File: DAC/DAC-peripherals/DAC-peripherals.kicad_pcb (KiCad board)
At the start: 2 copper layers, 46 parts, among them IC1 THS8135PHP, J1 Conn_01x04_Female, J2 Conn_01x02_Female, J3 Conn_01x11_Female, J4 Conn_01x11_Female, J5 Conn_01x11_Female, J6 Conn_01x01_Female, J7 Conn_01x01_Female, U1 SN74LV1T34DBV, U10 74LVC2T45DC, U11 74LVC2T45DC, U12 74LVC2T45DC, U13 74LVC2T45DC, U14 74LVC2T45DC, U15 74LVC2T45DC, U16 74LVC2T45DC, U2 74LVC2T45DC, U3 74LVC2T45DC, U4 74LVC2T45DC, U5 74LVC2T45DC, U6 74LVC2T45DC, U7 74LVC2T45DC, U8 74LVC2T45DC, U9 74LVC2T45DC

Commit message: improved PCB design
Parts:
- removed C10, C11, C12, C13, C14, C15, C16, C17, C18, C8, C9: C, Capacitor_SMD:C_0805_2012Metric
- removed J6, J7: Conn_01x01_Female, Connector_PinHeader_2.54mm:PinHeader_1x01_P2.54mm_Vertical
- removed U16: 74LVC2T45DC, Package_SO:VSSOP-8_2.3x2mm_P0.5mm
- added Q21: Q_NMOS_DGS, Package_TO_SOT_SMD:SOT-23, F.Cu at (122.2, 90.2)
- added R45: 10K, Resistor_SMD:R_0603_1608Metric, F.Cu at (120.2, 92.7)
- added R46: 10K, Resistor_SMD:R_0603_1608Metric, F.Cu at (121.9, 87.6)
- C1, C5, C6, C7: value C -> 100n; footprint Capacitor_SMD:C_0805_2012Metric -> Capacitor_SMD:C_0603_1608Metric
- C2, C3: value 0.1u -> 100n; footprint Capacitor_SMD:C_0805_2012Metric -> Capacitor_SMD:C_0603_1608Metric
- C4: value C -> 4.7u; footprint Capacitor_SMD:C_0805_2012Metric -> Capacitor_SMD:C_0603_1608Metric
- IC1: footprint THS8135PHP:QFP50P900X900X120-49N -> Package_QFP:TQFP-48-1EP_7x7mm_P0.5mm_EP5x5mm
- J1: value Conn_01x04_Female -> Conn_01x03_Female; footprint Connector_PinHeader_2.54mm:PinHeader_1x04_P2.54mm_Vertical -> Connector_PinSocket_2.54mm:PinSocket_1x03_P2.54mm_Vertical
- J2: value Conn_01x02_Female -> Conn_01x03_Female; footprint Connector_PinHeader_2.54mm:PinHeader_1x02_P2.54mm_Vertical -> Connector_PinSocket_2.54mm:PinSocket_1x03_P2.54mm_Vertical
- J3, J4: value Conn_01x11_Female -> Conn_01x10_Female; footprint Connector_PinHeader_2.54mm:PinHeader_1x11_P2.54mm_Vertical -> Connector_PinSocket_2.54mm:PinSocket_1x10_P2.54mm_Vertical
- J5: value Conn_01x11_Female -> Conn_01x08_Female; footprint Connector_PinHeader_2.54mm:PinHeader_1x11_P2.54mm_Vertical -> Connector_PinSocket_2.54mm:PinSocket_1x08_P2.54mm_Vertical
- R1: value 37.5 -> 2k; footprint Resistor_SMD:R_0805_2012Metric -> Resistor_SMD:R_0603_1608Metric
- R2, R3, R4: value NC -> 75; footprint Resistor_SMD:R_0805_2012Metric -> Resistor_SMD:R_0603_1608Metric
- U1: value SN74LV1T34DBV -> LK112M18TR
- moved J4 96.8 mm to (151.1, 112.5), turned to 180 degrees
- moved U2 89.7 mm to (143.8, 116.6), turned to -90 degrees
- moved U6 89.2 mm to (133.6, 116.6), turned to -90 degrees
- moved U5 88.8 mm to (146.1, 95.8), turned to 0 degrees
- moved U4 88.7 mm to (138.7, 116.6), turned to -90 degrees
- moved U3 87.9 mm to (146.1, 90.9), turned to 0 degrees
- moved U7 81.7 mm to (146.1, 100.8), turned to 0 degrees
- moved C6 79.4 mm to (138.4, 97.3)
- moved C5 76.5 mm to (137.7, 94.7), turned to 180 degrees
- moved U9 74.6 mm to (146.1, 106.2), turned to 0 degrees
- moved J3 74.3 mm to (122.2, 121.9), turned to 90 degrees
- moved U8 72.3 mm to (128.5, 116.6), turned to -90 degrees
- moved C1 71.5 mm to (132.3, 94.8), turned to 90 degrees
- moved U11 67.3 mm to (146.1, 111.0), turned to 0 degrees
- moved U10 61.2 mm to (123.4, 116.6), turned to -90 degrees
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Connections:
- net Net-(J3-Pad7) renamed /level_shifter_parallell_inv/level_shifter_2channel2/in2
- net Net-(J5-Pad5) renamed /level_shifter_parallell8/level_shifter_2channel7/in2
- C2 pad 2: Net-(C2-Pad2) -> GND
- C3 pad 1: GND -> +1V8
- C3 pad 2: Net-(C3-Pad2) -> GND
- C5 pad 2: GND -> Net-(C5-Pad2)
- C6 pad 1: +3.3V -> Net-(C6-Pad1)
- C7 pad 1: +3.3V -> Net-(C7-Pad1)
- IC1 pad 1: /Level Shifter B/B9 -> /B8
- IC1 pad 10: /Level Shifter B/B10 -> GND
- IC1 pad 11: GND -> +1V8
- IC1 pad 12: +1V8 -> GND
- IC1 pad 13: /Level Shifter R/B1 -> /R1
- IC1 pad 14: /Level Shifter R/B2 -> /R2
- IC1 pad 15: /Level Shifter R/B3 -> /R3
- IC1 pad 16: /Level Shifter R/B4 -> /R4
- IC1 pad 17: /Level Shifter R/B5 -> /R5
- IC1 pad 18: /Level Shifter R/B6 -> /R6
- IC1 pad 19: /Level Shifter R/B7 -> /R7
- IC1 pad 2: /Level Shifter B/B8 -> /B7
- IC1 pad 20: /Level Shifter R/B8 -> /R8
- IC1 pad 21: /Level Shifter R/B9 -> /R9
- IC1 pad 22: /Level Shifter R/B10 -> /R10
- IC1 pad 23: +3.3V -> +1V8
- IC1 pad 24: +3.3V -> +1V8
- IC1 pad 25: +3.3V -> +1V8
- IC1 pad 26: Net-(IC1-Pad26) -> /CLK
- IC1 pad 27: /Level Shifter G/B9 -> /G10
- IC1 pad 28: /Level Shifter G/B8 -> /G9
- IC1 pad 29: /Level Shifter G/B7 -> /G8
- IC1 pad 3: /Level Shifter B/B7 -> /B6
- IC1 pad 30: /Level Shifter G/B6 -> /G7
- IC1 pad 31: /Level Shifter G/B5 -> /G6
- IC1 pad 32: /Level Shifter G/B4 -> /G5
- IC1 pad 33: /Level Shifter G/B3 -> /G4
- IC1 pad 34: /Level Shifter G/B2 -> /G3
- IC1 pad 35: /Level Shifter G/B1 -> /G2
- IC1 pad 36: /Level Shifter G/B10 -> /G1
- IC1 pad 37: Net-(C3-Pad2) -> Net-(C6-Pad1)
- IC1 pad 38: Net-(R1-Pad2) -> /FSADJ
- IC1 pad 39: Net-(C2-Pad2) -> Net-(C5-Pad2)
- IC1 pad 4: /Level Shifter B/B6 -> /B5
- IC1 pad 41: Net-(IC1-Pad41) -> /out_y
- IC1 pad 43: Net-(IC1-Pad43) -> /out_x
- IC1 pad 45: Net-(IC1-Pad45) -> /out_i
- IC1 pad 49: unconnected-(IC1-Pad49) -> GND
- IC1 pad 5: /Level Shifter B/B5 -> /B4
- IC1 pad 6: /Level Shifter B/B4 -> /B3
- IC1 pad 7: /Level Shifter B/B3 -> /B2
- IC1 pad 8: /Level Shifter B/B2 -> /B1
- IC1 pad 9: /Level Shifter B/B1 -> GND
- J1 pad 2: Net-(IC1-Pad45) -> /CLK_in
- J1 pad 3: Net-(IC1-Pad43) -> +3.3V
- J2 pad 1: GND -> /out_x
- J2 pad 2: Net-(U1-Pad2) -> /out_y
- J3 pad 1: unconnected-(J3-Pad1) -> /level_shifter_parallell_inv/level_shifter_2channel5/in2
- J3 pad 10: Net-(J3-Pad10) -> /level_shifter_parallell_inv/level_shifter_2channel1/in1
- J3 pad 2: Net-(J3-Pad2) -> /level_shifter_parallell_inv/level_shifter_2channel5/in1
- J3 pad 3: Net-(J3-Pad3) -> /level_shifter_parallell_inv/level_shifter_2channel4/in2
- J3 pad 4: Net-(J3-Pad4) -> /level_shifter_parallell_inv/level_shifter_2channel4/in1
- J3 pad 5: Net-(J3-Pad5) -> /level_shifter_parallell_inv/level_shifter_2channel3/in2
- J3 pad 6: Net-(J3-Pad6) -> /level_shifter_parallell_inv/level_shifter_2channel3/in1
- J3 pad 8: Net-(J3-Pad8) -> /level_shifter_parallell_inv/level_shifter_2channel2/in1
- J3 pad 9: Net-(J3-Pad9) -> /level_shifter_parallell_inv/level_shifter_2channel1/in2
- J4 pad 1: unconnected-(J4-Pad1) -> /level_shifter_parallell1/level_shifter_2channel5/in2
- J4 pad 10: Net-(J4-Pad10) -> /level_shifter_parallell1/level_shifter_2channel1/in1
- J4 pad 2: Net-(J4-Pad2) -> /level_shifter_parallell1/level_shifter_2channel5/in1
- J4 pad 3: Net-(J4-Pad3) -> /level_shifter_parallell1/level_shifter_2channel4/in2
- J4 pad 4: Net-(J4-Pad4) -> /level_shifter_parallell1/level_shifter_2channel4/in1
- J4 pad 5: Net-(J4-Pad5) -> /level_shifter_parallell1/level_shifter_2channel3/in2
- J4 pad 6: Net-(J4-Pad6) -> /level_shifter_parallell1/level_shifter_2channel3/in1
- J4 pad 7: Net-(J4-Pad7) -> /level_shifter_parallell1/level_shifter_2channel2/in2
- J4 pad 8: Net-(J4-Pad8) -> /level_shifter_parallell1/level_shifter_2channel2/in1
- J4 pad 9: Net-(J4-Pad9) -> /level_shifter_parallell1/level_shifter_2channel1/in2
- J5 pad 1: unconnected-(J5-Pad1) -> /level_shifter_parallell8/level_shifter_2channel9/in2
- J5 pad 2: Net-(J5-Pad2) -> /level_shifter_parallell8/level_shifter_2channel9/in1
- J5 pad 3: Net-(J5-Pad3) -> /level_shifter_parallell8/level_shifter_2channel8/in2
- J5 pad 4: Net-(J5-Pad4) -> /level_shifter_parallell8/level_shifter_2channel8/in1
- J5 pad 6: Net-(J5-Pad6) -> /level_shifter_parallell8/level_shifter_2channel7/in1
- J5 pad 7: Net-(J5-Pad7) -> /level_shifter_parallell8/level_shifter_2channel6/in2
- J5 pad 8: Net-(J5-Pad8) -> /level_shifter_parallell8/level_shifter_2channel6/in1
- R1 pad 1: GND -> /FSADJ
- R1 pad 2: Net-(R1-Pad2) -> GND
- R2 pad 1: GND -> /out_i
- R2 pad 2: Net-(IC1-Pad45) -> GND
- R3 pad 1: GND -> /out_y
- R3 pad 2: Net-(IC1-Pad43) -> GND
- R4 pad 1: Net-(IC1-Pad41) -> /out_x
- U1 pad 1: unconnected-(U1-Pad1) -> +3.3V
- U1 pad 2: Net-(U1-Pad2) -> GND
- U1 pad 3: GND -> Net-(C7-Pad1)
- U1 pad 4: Net-(IC1-Pad26) -> +1V8
- U10 pad 1: +3.3V -> +1V8
- U10 pad 2: /Level Shifter B/B7 -> /R2
- U10 pad 3: /Level Shifter B/B8 -> /R1
- U10 pad 6: Net-(J4-Pad9) -> /level_shifter_parallell_inv/level_shifter_2channel5/in2
- U10 pad 7: Net-(J4-Pad8) -> /level_shifter_parallell_inv/level_shifter_2channel5/in1
- U11 pad 1: +3.3V -> +1V8
- U11 pad 2: /Level Shifter B/B9 -> /G9
- U11 pad 3: /Level Shifter B/B10 -> /G10
- U11 pad 6: Net-(J4-Pad11) -> /level_shifter_parallell1/level_shifter_2channel5/in2
- U11 pad 7: Net-(J4-Pad10) -> /level_shifter_parallell1/level_shifter_2channel5/in1
- U12 pad 1: +3.3V -> +1V8
- U12 pad 2: /Level Shifter G/B1 -> /B1
- U12 pad 3: /Level Shifter G/B2 -> /B2
- U12 pad 6: Net-(J5-Pad3) -> /level_shifter_parallell8/level_shifter_2channel6/in2
- U12 pad 7: Net-(J5-Pad2) -> /level_shifter_parallell8/level_shifter_2channel6/in1
- U13 pad 1: +3.3V -> +1V8
- U13 pad 2: /Level Shifter G/B3 -> /B3
- U13 pad 3: /Level Shifter G/B4 -> /B4
- U13 pad 7: Net-(J5-Pad4) -> /level_shifter_parallell8/level_shifter_2channel7/in1
- U14 pad 1: +3.3V -> +1V8
- U14 pad 2: /Level Shifter G/B5 -> /B5
- U14 pad 3: /Level Shifter G/B6 -> /B6
- U14 pad 6: Net-(J5-Pad7) -> /level_shifter_parallell8/level_shifter_2channel8/in2
- U14 pad 7: Net-(J5-Pad6) -> /level_shifter_parallell8/level_shifter_2channel8/in1
- U15 pad 1: +3.3V -> +1V8
- U15 pad 2: /Level Shifter G/B7 -> /B7
- U15 pad 3: /Level Shifter G/B8 -> /B8
- U15 pad 6: Net-(J5-Pad9) -> /level_shifter_parallell8/level_shifter_2channel9/in2
- U15 pad 7: Net-(J5-Pad8) -> /level_shifter_parallell8/level_shifter_2channel9/in1
- U2 pad 1: +3.3V -> +1V8
- U2 pad 2: /Level Shifter R/B1 -> /R10
- U2 pad 3: /Level Shifter R/B2 -> /R9
- U2 pad 6: Net-(J3-Pad3) -> /level_shifter_parallell_inv/level_shifter_2channel1/in2
- U2 pad 7: Net-(J3-Pad2) -> /level_shifter_parallell_inv/level_shifter_2channel1/in1
- U3 pad 1: +3.3V -> +1V8
- U3 pad 2: /Level Shifter R/B3 -> /G1
- U3 pad 3: /Level Shifter R/B4 -> /G2
- U3 pad 6: Net-(J3-Pad5) -> /level_shifter_parallell1/level_shifter_2channel1/in2
- U3 pad 7: Net-(J3-Pad4) -> /level_shifter_parallell1/level_shifter_2channel1/in1
- U4 pad 1: +3.3V -> +1V8
- U4 pad 2: /Level Shifter R/B5 -> /R8
- U4 pad 3: /Level Shifter R/B6 -> /R7
- U4 pad 7: Net-(J3-Pad6) -> /level_shifter_parallell_inv/level_shifter_2channel2/in1
- U5 pad 1: +3.3V -> +1V8
- U5 pad 2: /Level Shifter R/B7 -> /G3
- U5 pad 3: /Level Shifter R/B8 -> /G4
- U5 pad 6: Net-(J3-Pad9) -> /level_shifter_parallell1/level_shifter_2channel2/in2
- U5 pad 7: Net-(J3-Pad8) -> /level_shifter_parallell1/level_shifter_2channel2/in1
- U6 pad 1: +3.3V -> +1V8
- U6 pad 2: /Level Shifter R/B9 -> /R6
- U6 pad 3: /Level Shifter R/B10 -> /R5
- U6 pad 6: Net-(J3-Pad11) -> /level_shifter_parallell_inv/level_shifter_2channel3/in2
- U6 pad 7: Net-(J3-Pad10) -> /level_shifter_parallell_inv/level_shifter_2channel3/in1
- U7 pad 1: +3.3V -> +1V8
- U7 pad 2: /Level Shifter B/B1 -> /G5
- U7 pad 3: /Level Shifter B/B2 -> /G6
- U7 pad 6: Net-(J4-Pad3) -> /level_shifter_parallell1/level_shifter_2channel3/in2
- U7 pad 7: Net-(J4-Pad2) -> /level_shifter_parallell1/level_shifter_2channel3/in1
- U8 pad 1: +3.3V -> +1V8
- U8 pad 2: /Level Shifter B/B3 -> /R4
- U8 pad 3: /Level Shifter B/B4 -> /R3
- U8 pad 6: Net-(J4-Pad5) -> /level_shifter_parallell_inv/level_shifter_2channel4/in2
- U8 pad 7: Net-(J4-Pad4) -> /level_shifter_parallell_inv/level_shifter_2channel4/in1
- U9 pad 1: +3.3V -> +1V8
- U9 pad 2: /Level Shifter B/B5 -> /G7
- U9 pad 3: /Level Shifter B/B6 -> /G8
- U9 pad 6: Net-(J4-Pad7) -> /level_shifter_parallell1/level_shifter_2channel4/in2
- U9 pad 7: Net-(J4-Pad6) -> /level_shifter_parallell1/level_shifter_2channel4/in1
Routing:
- net GND: track 254.9 -> 0.00 mm, vias 23 -> 18
- net +3.3V: track 299.9 -> 48.1 mm, vias 6 -> 33
- net /CLK: track 0.00 -> 44.9 mm, vias 0 -> 2
- net /Level Shifter B/B10: track 35.9 -> 0.00 mm, vias 2 -> 0
- net +1V8: track 19.6 -> 51.0 mm, vias 0 -> 34
- net /Level Shifter R/B1: track 29.7 -> 0.00 mm, vias 2 -> 0
- net /Level Shifter R/B10: track 27.1 -> 0.00 mm, vias 2 -> 0
- net /Level Shifter R/B9: track 26.8 -> 0.00 mm, vias 2 -> 0
- net /Level Shifter R/B2: track 26.7 -> 0.00 mm, vias 2 -> 0
- net /Level Shifter G/B10: track 25.8 -> 0.00 mm, vias 2 -> 0
- net /Level Shifter R/B8: track 21.9 -> 0.00 mm, vias 2 -> 0
- net /Level Shifter R/B3: track 21.8 -> 0.00 mm, vias 2 -> 0
- net /Level Shifter R/B6: track 21.6 -> 0.00 mm, vias 2 -> 0
- net /FSADJ: track 0.00 -> 21.1 mm
- net Net-(IC1-Pad45): track 20.9 -> 0.00 mm, vias 2 -> 0
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- added copper zone on In1.Cu, net +1V8
- added copper zone on In1.Cu, net +3.3V
- added copper zone on In2.Cu, net GND
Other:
- board outline added: 43.2 x 48.5 mm
- copper layers 2 -> 4

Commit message: improved PCB design again
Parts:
- moved C5 2.03 mm to (137.7, 92.7)
- moved C1 0.53 mm to (132.3, 94.2)
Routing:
- net /R10: track 0.00 -> 13.7 mm
- net /CLK_in: track 3.39 -> 14.5 mm
- net +3.3V: track 48.1 -> 54.7 mm, vias 33 -> 36
- net Net-(C5-Pad2): track 4.54 -> 6.06 mm
- net +1V8: track 51.0 -> 51.7 mm
- net GND: vias 18 -> 23

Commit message: improved PCB again again
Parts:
- J2: value Conn_01x03_Female -> Conn_02x03_Odd_Even; footprint Connector_PinSocket_2.54mm:PinSocket_1x03_P2.54mm_Vertical -> Connector_PinSocket_2.54mm:PinSocket_2x03_P2.54mm_Vertical
- moved R2 7.26 mm to (131.7, 86.1)
- moved R4 7.24 mm to (136.9, 86.1)
- moved R3 7.18 mm to (134.4, 86.0)
- renumbered C7 to C5, C5 to C6, C6 to C7, Q21 to Q1, R45 to R5, R46 to R6, U15 to U10, U4 to U3, U6 to U4, U8 to U5, U10 to U6, U12 to U7, U13 to U8, U14 to U9
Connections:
- J2 pad 2: /out_y -> GND
- J2 pad 3: /out_i -> /out_y
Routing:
- net +3.3V: track 54.7 -> 60.5 mm, vias 36 -> 37
- net /out_y: track 20.2 -> 19.2 mm
- net /out_x: track 20.8 -> 20.1 mm
- net /out_i: track 20.1 -> 19.4 mm
- net GND: vias 23 -> 19

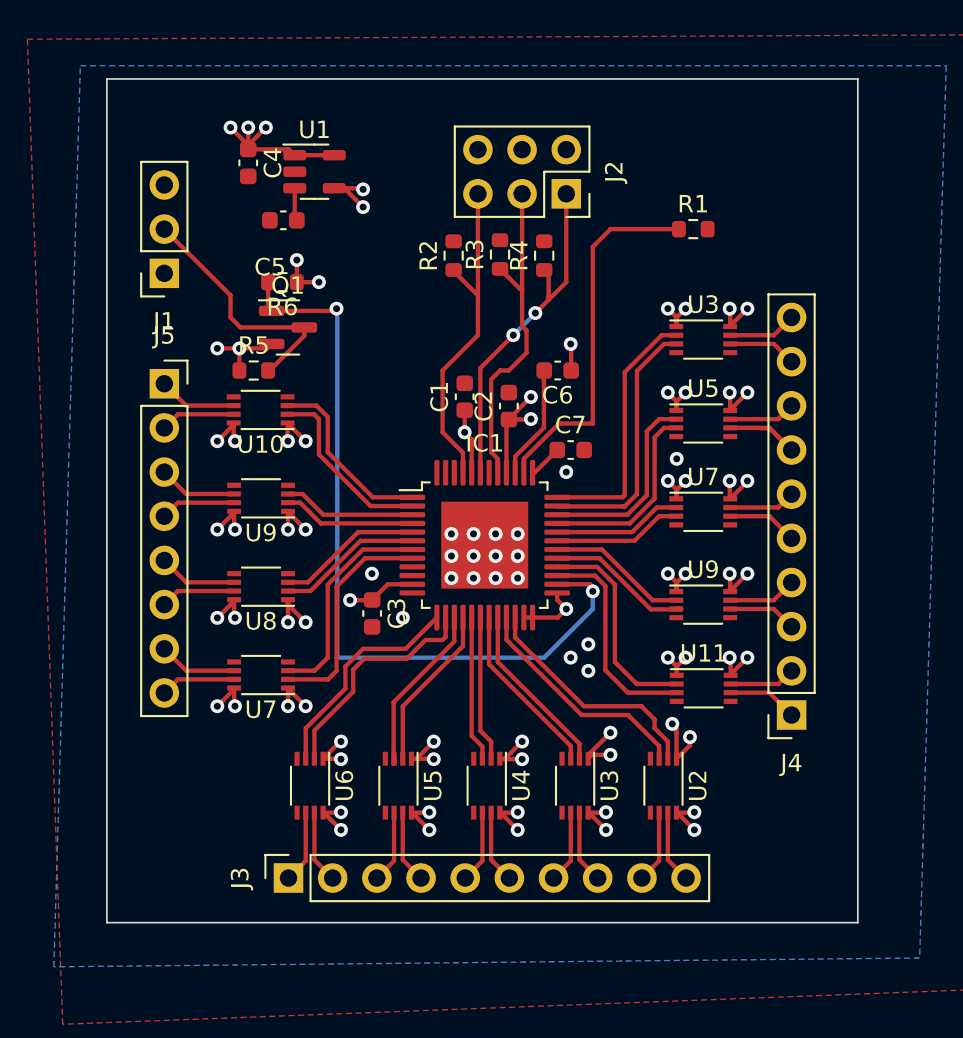
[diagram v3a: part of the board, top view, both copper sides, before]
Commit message: added pin descriptions to silkscreen
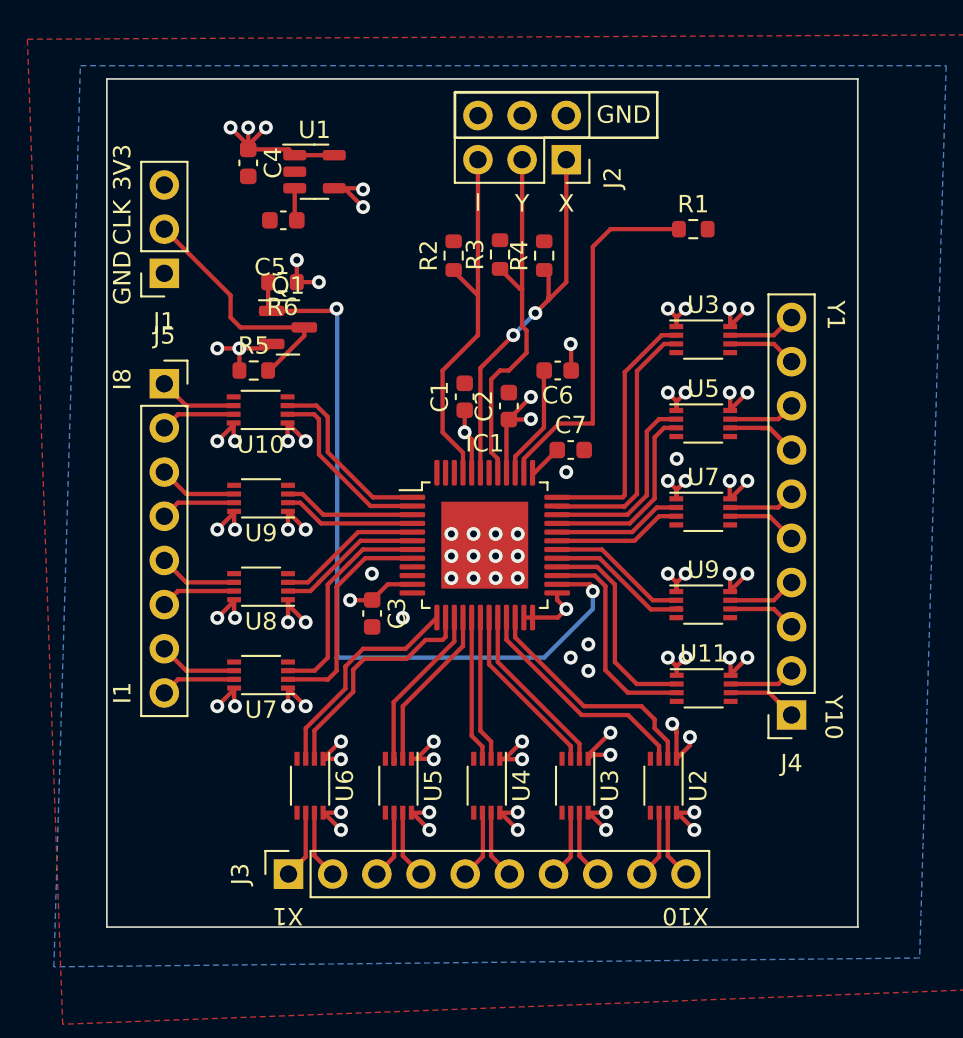
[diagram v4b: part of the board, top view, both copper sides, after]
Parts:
- moved J2 1.96 mm to (138.2, 80.6)
- moved J3 0.23 mm to (122.2, 121.7)
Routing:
- net /out_i: track 19.4 -> 21.4 mm
- net /out_y: track 19.2 -> 21.1 mm
- net /out_x: track 20.1 -> 22.0 mm
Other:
- board size 43.2 x 48.5 mm -> 43.2 x 48.8 mm
- board text added: "3V3"
- board text added: "CLK"
- board text added: "GND"
- board text added: "I"
- board text added: "I1"
- board text added: "I8"
- board text added: "X"
- board text added: "X1"
- board text added: "X10"
- board text added: "Y"
- board text added: "Y1"
- board text added: "Y10"

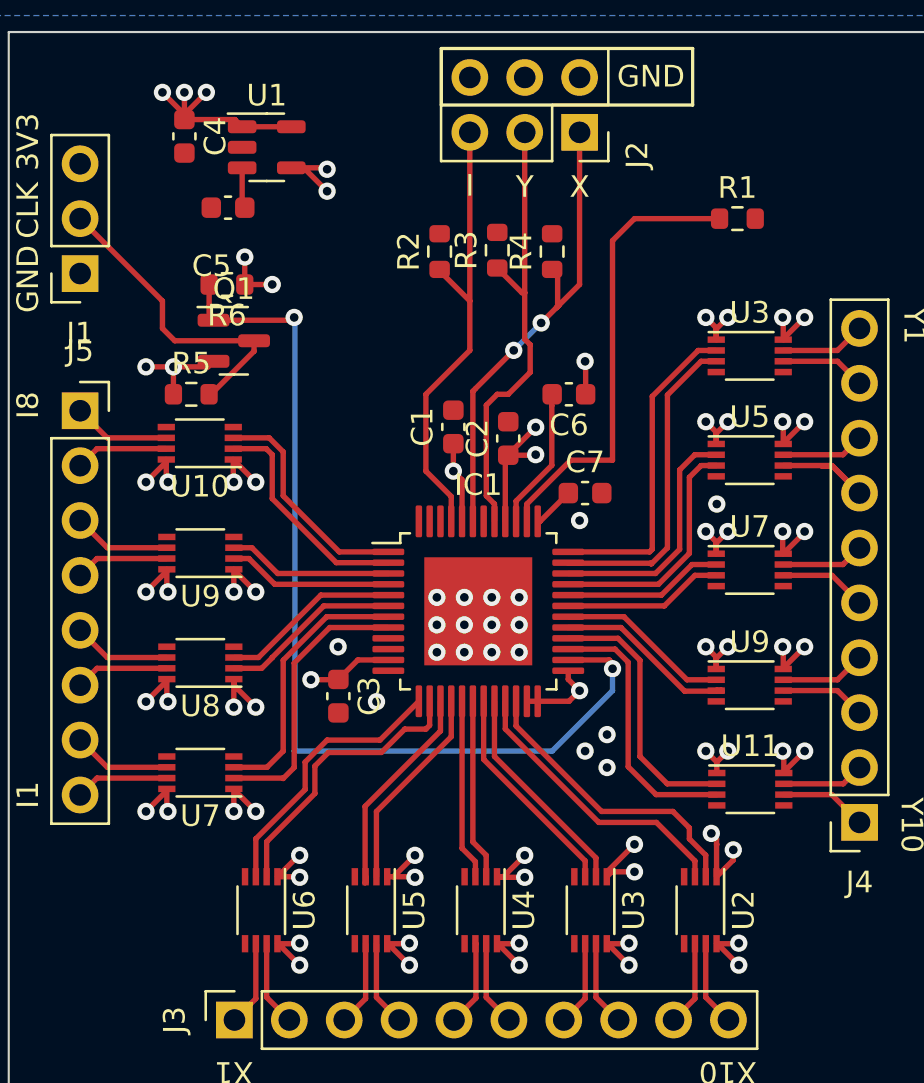
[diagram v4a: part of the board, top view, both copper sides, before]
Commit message: added more gnd vias
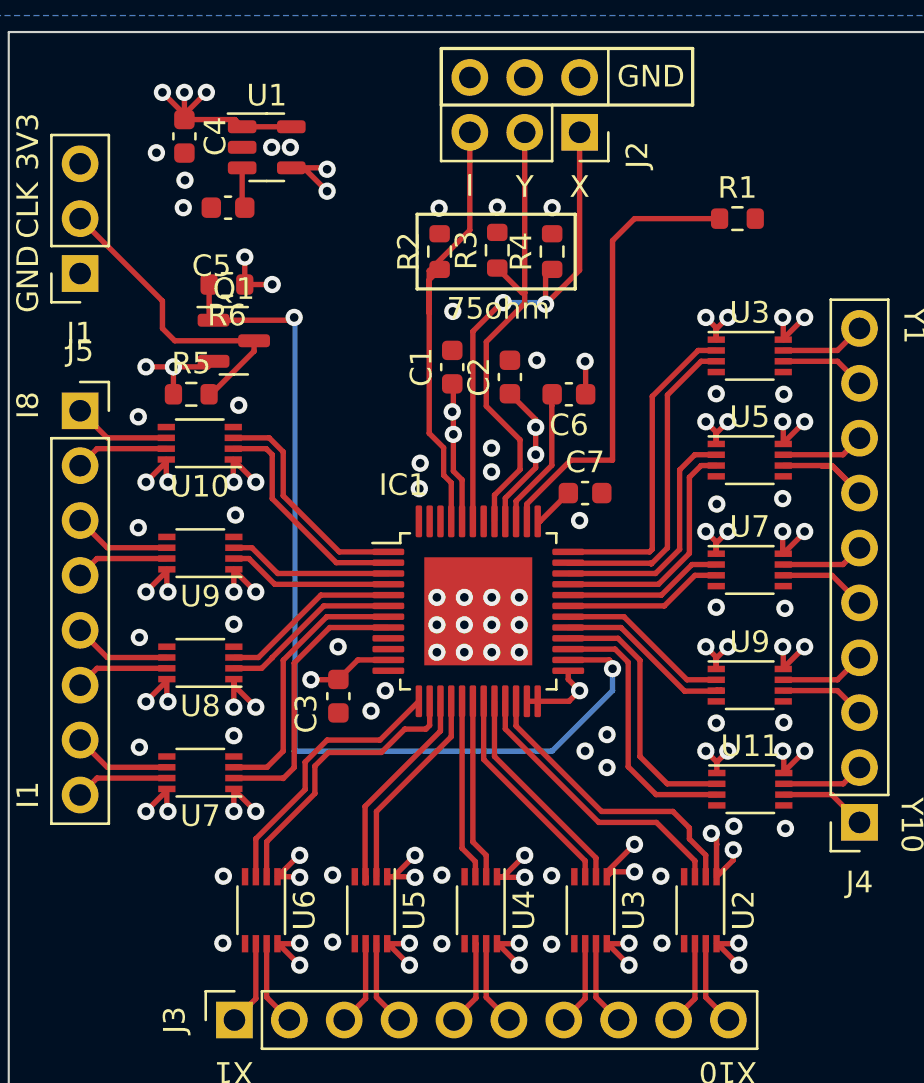
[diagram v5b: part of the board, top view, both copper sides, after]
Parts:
- moved C2 2.85 mm to (135.0, 91.9)
- moved C1 2.77 mm to (132.3, 91.5)
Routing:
- net +3.3V: track 60.5 -> 64.3 mm, vias 37 -> 38
- net /out_x: track 22.0 -> 23.1 mm
- net GND: vias 19 -> 61
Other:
- board text added: "75ohm"
